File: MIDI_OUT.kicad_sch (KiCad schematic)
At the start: 3 parts, among them J29 Conn_01x03

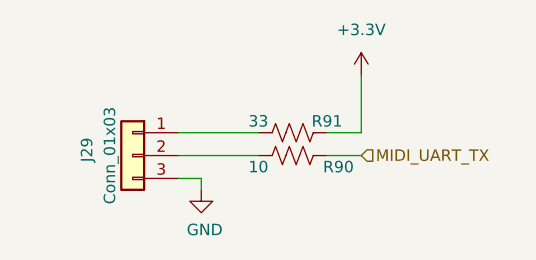
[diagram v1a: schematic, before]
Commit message: simplified design, rely on external boards more to cover those cases
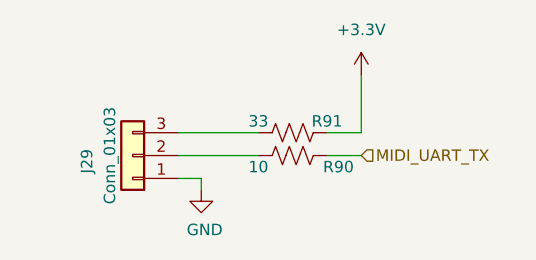
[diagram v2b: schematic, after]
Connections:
- net GND: now also J29.1 (Pin_1); no longer J29.3 (Pin_3)
- net at R91.2: now also J29.3 (Pin_3); no longer J29.1 (Pin_1)
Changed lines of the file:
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@@
+    )
+  )
+  (symbol (lib_id "4ms_Connector:Conn_01x03") (at 129.54 72.39 180) (unit 1)
+    (in_bom yes) (on_board yes) (dnp no)
+    (property "Reference" "J29" (at 124.46 73.025 90)
+      (effects (font (size 1.27 1.27)))
+    )
+    (property "Value" "Conn_01x03" (at 127 72.39 90)
+      (effects (font (size 1.27 1.27)))
+    )
+    (property "Footprint" "Ultralibrarian:PinHeader_1x03_P2.54mm_Vertical_Female" (at 129.54 79.375 0)
+      (effects (font (size 1.27 1.27)) hide)
+    )
+    (property "Datasheet" "" (at 129.54 72.39 0)
+      (effects (font (size 1.27 1.27)) hide)
+    )
+    (property "Specifications" "HEADER 1x3 MALE PINS 0.100” 180deg" (at 132.08 64.516 0)
+      (effects (font (size 1.27 1.27)) (justify left) hide)
+    )
+    (property "Manufacturer" "TAD" (at 132.08 62.992 0)
+      (effects (font (size 1.27 1.27)) (justify left) hide)
+    )
+    (property "Part Number" "1-0301FBV0T" (at 132.08 61.468 0)
+      (effects (font (size 1.27 1.27)) (justify left) hide)
+    )
+    (pin "1")
+    (pin "2")
+    (pin "3")
+    (instances
+      (project "DaisySeedBreakout"
+        (path "/a83c9f4b-f61b-47d4-b39d-4636bff6eb0e"
+          (reference "J29") (unit 1)
+        )
+        (path "/a83c9f4b-f61b-47d4-b39d-4636bff6eb0e/8edb4e87-22fe-4415-a59d-3c6e3164f7d2"
+          (reference "J1") (unit 1)
+        )
+      )
     )
   )
@@
         )
       )
-    )
-  )
-  (symbol (lib_id "4ms_Connector:Conn_01x03") (at 129.54 72.39 0) (mirror y) (unit 1)
-    (in_bom yes) (on_board yes) (dnp no)
-    (property "Reference" "J29" (at 124.46 71.755 90)
-      (effects (font (size 1.27 1.27)))
-    )
-    (property "Value" "Conn_01x03" (at 127 72.39 90)
-      (effects (font (size 1.27 1.27)))
-    )
-    (property "Footprint" "Ultralibrarian:PinHeader_1x03_P2.54mm_Vertical_Female" (at 129.54 65.405 0)
-      (effects (font (size 1.27 1.27)) hide)
-    )
-    (property "Datasheet" "" (at 129.54 72.39 0)
-      (effects (font (size 1.27 1.27)) hide)
-    )
-    (property "Specifications" "HEADER 1x3 MALE PINS 0.100” 180deg" (at 132.08 80.264 0)
-      (effects (font (size 1.27 1.27)) (justify left) hide)
-    )
-    (property "Manufacturer" "TAD" (at 132.08 81.788 0)
-      (effects (font (size 1.27 1.27)) (justify left) hide)
-    )
-    (property "Part Number" "1-0301FBV0T" (at 132.08 83.312 0)
-      (effects (font (size 1.27 1.27)) (justify left) hide)
-    )
-    (pin "1")
-    (pin "2")
-    (pin "3")
-    (instances
-      (project "DaisySeedBreakout"
-        (path "/a83c9f4b-f61b-47d4-b39d-4636bff6eb0e"
-          (reference "J29") (unit 1)
-        )
-        (path "/a83c9f4b-f61b-47d4-b39d-4636bff6eb0e/8edb4e87-22fe-4415-a59d-3c6e3164f7d2"
-          (reference "J1") (unit 1)
-        )
-      )

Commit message: periodic update
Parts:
- J29: footprint Ultralibrarian:PinHeader_1x03_P2.54mm_Vertical_Female -> HeadersWithSolderHoles:PinHeader_1x03_P2.54mm_Vertical_Female_WithSolderHoles
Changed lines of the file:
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@@
       (effects (font (size 1.27 1.27)))
     )
-    (property "Footprint" "Ultralibrarian:PinHeader_1x03_P2.54mm_Vertical_Female" (at 129.54 79.375 0)
+    (property "Footprint" "HeadersWithSolderHoles:PinHeader_1x03_P2.54mm_Vertical_Female_WithSolderHoles" (at 129.54 79.375 0)
       (effects (font (size 1.27 1.27)) hide)
     )

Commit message: Layout routed, no DRC yet
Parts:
- J29: footprint HeadersWithSolderHoles:PinHeader_1x03_P2.54mm_Vertical_Female_WithSolderHoles -> FemaleHeaders:PinHeader_1x03_P2.54mm_Vertical_Female
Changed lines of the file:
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@@
       (effects (font (size 1.27 1.27)))
     )
-    (property "Footprint" "HeadersWithSolderHoles:PinHeader_1x03_P2.54mm_Vertical_Female_WithSolderHoles" (at 129.54 79.375 0)
+    (property "Footprint" "FemaleHeaders:PinHeader_1x03_P2.54mm_Vertical_Female" (at 129.54 79.375 0)
       (effects (font (size 1.27 1.27)) hide)
     )

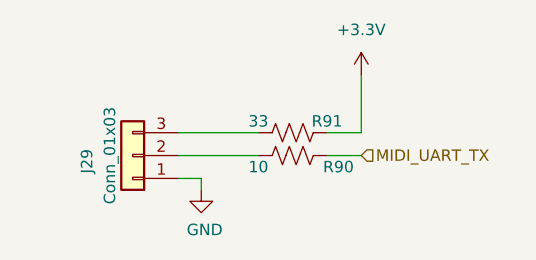
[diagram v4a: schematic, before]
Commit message: PCB cleanup, added accelerometer as easy sensor to begin with
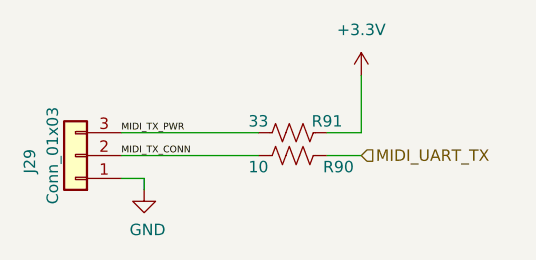
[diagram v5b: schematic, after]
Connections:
- net MIDI_TX_CONN: now reaches J29.2 (Pin_2), R90.2
- net MIDI_TX_PWR: now reaches J29.3 (Pin_3), R91.2
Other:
- moved on the sheet: J29
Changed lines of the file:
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@@
 (kicad_sch (version 20230121) (generator eeschema)
   (paper "A4")
-  (wire (pts (xy 137.16 74.93) (xy 137.16 76.2))
+  (wire (pts (xy 130.81 74.93) (xy 130.81 76.2))
     (stroke (width 0) (type default))
   )
@@
     (stroke (width 0) (type default))
   )
-  (wire (pts (xy 134.62 74.93) (xy 137.16 74.93))
+  (wire (pts (xy 128.27 74.93) (xy 130.81 74.93))
     (stroke (width 0) (type default))
   )
-  (wire (pts (xy 134.62 72.39) (xy 143.51 72.39))
+  (wire (pts (xy 128.27 72.39) (xy 143.51 72.39))
     (stroke (width 0) (type default))
   )
-  (wire (pts (xy 134.62 69.85) (xy 143.51 69.85))
+  (wire (pts (xy 128.27 69.85) (xy 143.51 69.85))
     (stroke (width 0) (type default))
+  )
+  (label "MIDI_TX_CONN" (at 128.27 72.39 0) (fields_autoplaced)
+    (effects (font (size 0.75 0.75)) (justify left bottom))
+  )
+  (label "MIDI_TX_PWR" (at 128.27 69.85 0) (fields_autoplaced)
+    (effects (font (size 0.75 0.75)) (justify left bottom))
   )
   (hierarchical_label "MIDI_UART_TX" (shape input) (at 154.94 72.39 0) (fields_autoplaced)
@@
     )
   )
-  (symbol (lib_id "4ms_Connector:Conn_01x03") (at 129.54 72.39 180) (unit 1)
+  (symbol (lib_id "4ms_Connector:Conn_01x03") (at 123.19 72.39 180) (unit 1)
     (in_bom yes) (on_board yes) (dnp no)
-    (property "Reference" "J29" (at 124.46 73.025 90)
+    (property "Reference" "J29" (at 118.11 73.025 90)
       (effects (font (size 1.27 1.27)))
     )
-    (property "Value" "Conn_01x03" (at 127 72.39 90)
+    (property "Value" "Conn_01x03" (at 120.65 72.39 90)
       (effects (font (size 1.27 1.27)))
     )
-    (property "Footprint" "FemaleHeaders:PinHeader_1x03_P2.54mm_Vertical_Female" (at 129.54 79.375 0)
+    (property "Footprint" "FemaleHeaders:PinHeader_1x03_P2.54mm_Vertical_Female" (at 123.19 79.375 0)
       (effects (font (size 1.27 1.27)) hide)
     )
-    (property "Datasheet" "" (at 129.54 72.39 0)
+    (property "Datasheet" "" (at 123.19 72.39 0)
       (effects (font (size 1.27 1.27)) hide)
     )
-    (property "Specifications" "HEADER 1x3 MALE PINS 0.100” 180deg" (at 132.08 64.516 0)
+    (property "Specifications" "HEADER 1x3 MALE PINS 0.100” 180deg" (at 125.73 64.516 0)
       (effects (font (size 1.27 1.27)) (justify left) hide)
     )
-    (property "Manufacturer" "TAD" (at 132.08 62.992 0)
+    (property "Manufacturer" "TAD" (at 125.73 62.992 0)
       (effects (font (size 1.27 1.27)) (justify left) hide)
     )
-    (property "Part Number" "1-0301FBV0T" (at 132.08 61.468 0)
+    (property "Part Number" "1-0301FBV0T" (at 125.73 61.468 0)
       (effects (font (size 1.27 1.27)) (justify left) hide)
     )
@@
     )
   )
-  (symbol (lib_id "power:GND") (at 137.16 76.2 0) (unit 1)
+  (symbol (lib_id "power:GND") (at 130.81 76.2 0) (unit 1)
     (in_bom yes) (on_board yes) (dnp no)
-    (property "Reference" "#PWR064" (at 137.16 82.55 0)
+    (property "Reference" "#PWR064" (at 130.81 82.55 0)
       (effects (font (size 1.27 1.27)) hide)
     )
-    (property "Value" "GND" (at 137.541 80.645 0)
+    (property "Value" "GND" (at 131.191 80.645 0)
       (effects (font (size 1.27 1.27)))
     )
-    (property "Footprint" "" (at 137.16 76.2 0)
+    (property "Footprint" "" (at 130.81 76.2 0)
       (effects (font (size 1.27 1.27)) hide)
     )
-    (property "Datasheet" "" (at 137.16 76.2 0)
+    (property "Datasheet" "" (at 130.81 76.2 0)
       (effects (font (size 1.27 1.27)) hide)
     )
